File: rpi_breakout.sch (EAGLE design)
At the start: 31 parts, among them Q1 BSS138, Q2 BSS138, U2 TXB0108, U3 TXB0108

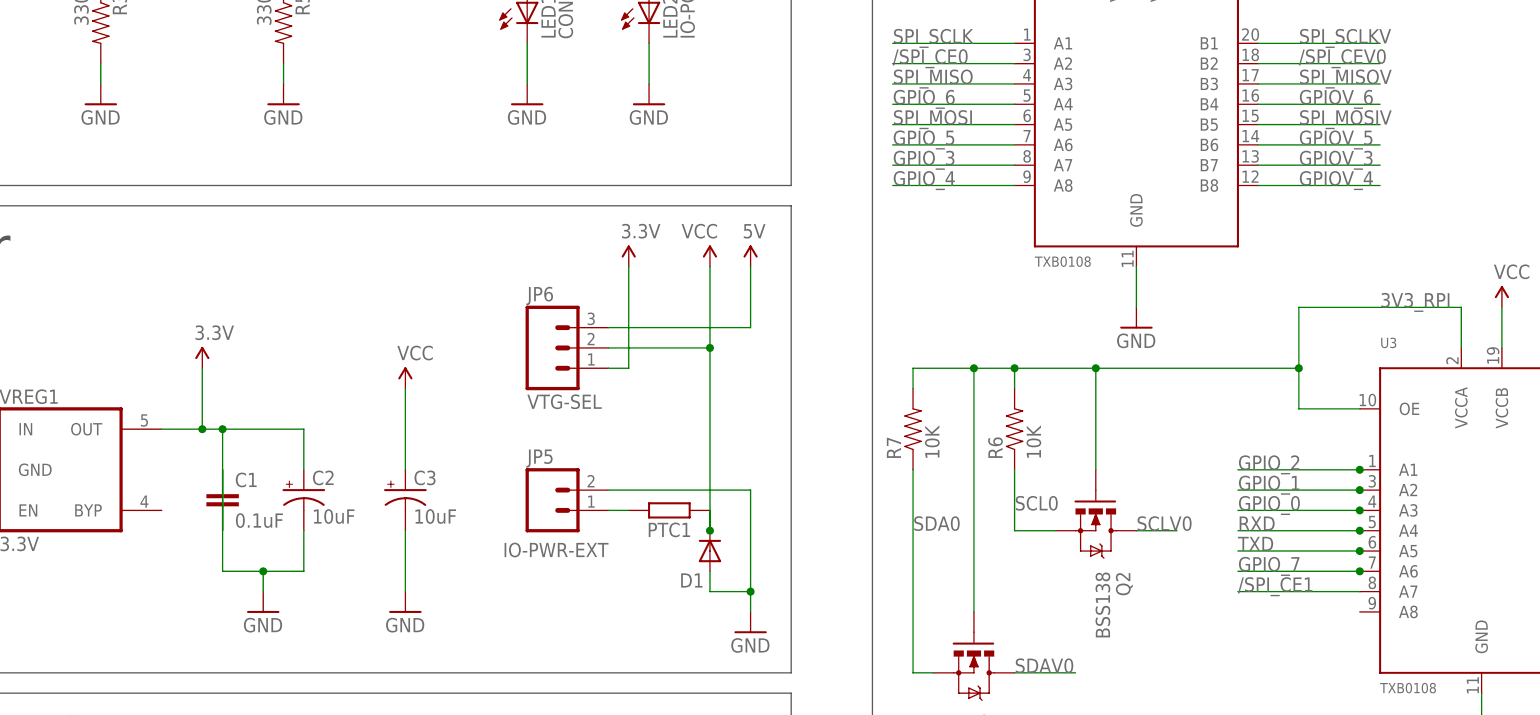
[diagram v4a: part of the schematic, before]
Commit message: Cleanup/routing after adding I2C-friendly level converter.
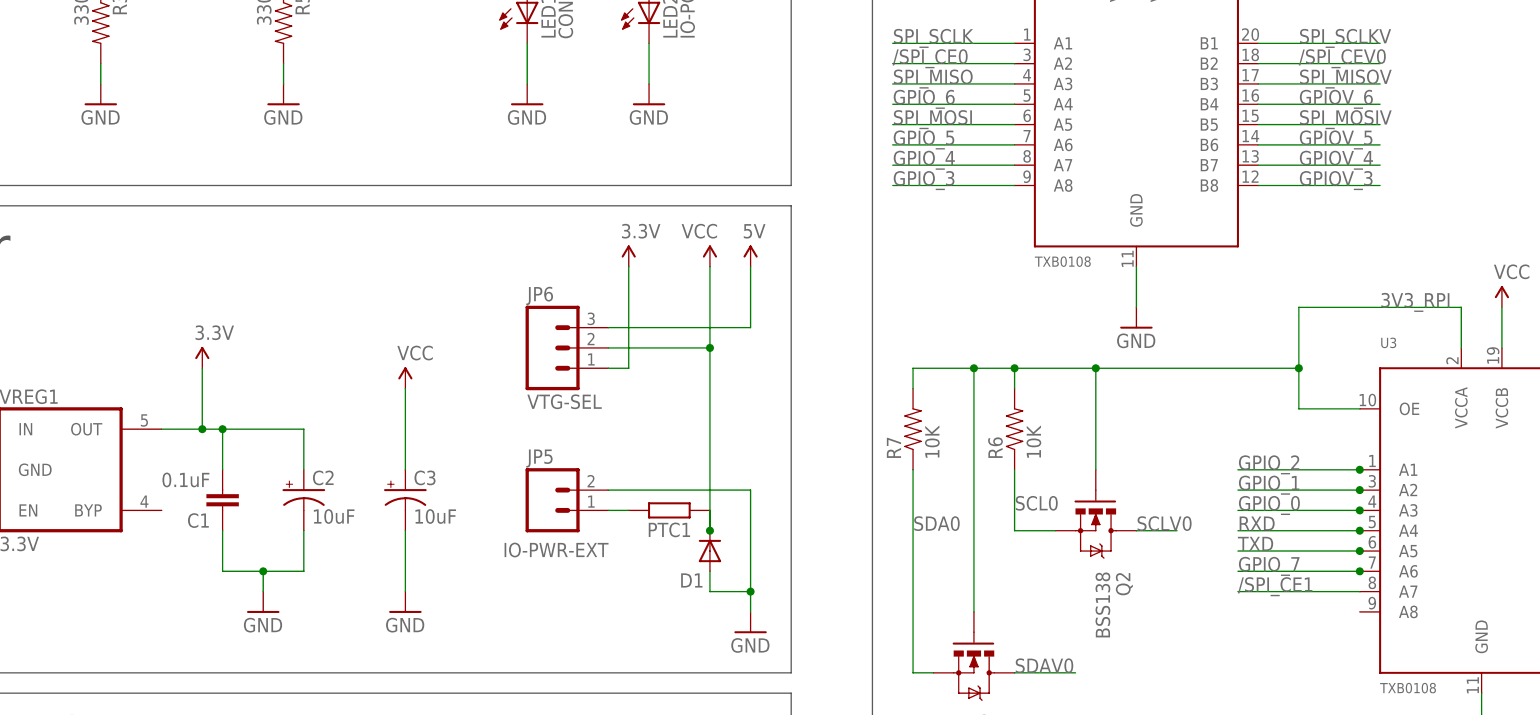
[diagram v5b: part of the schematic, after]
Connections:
- net GPIOV_3: now also U2.B8; no longer U2.B7
- net GPIOV_4: now also U2.B7; no longer U2.B8
- net GPIO_3: now also U2.A8; no longer U2.A7
- net GPIO_4: now also U2.A7; no longer U2.A8
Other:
- moved on the sheet: C1
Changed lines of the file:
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@@
 <instance part="GND8" gate="1" x="208.28" y="53.34"/>
 <instance part="VREG1" gate="G$1" x="30.48" y="88.9"/>
-<instance part="C1" gate="G$1" x="50.8" y="83.82"/>
+<instance part="C1" gate="G$1" x="50.8" y="86.36" rot="R180"/>
 <instance part="C2" gate="G$1" x="60.96" y="86.36"/>
 <instance part="GND9" gate="1" x="55.88" y="71.12"/>
@@
 <wire x1="55.88" y1="76.2" x2="55.88" y2="73.66" width="0.1524" layer="91"/>
 <pinref part="C1" gate="G$1" pin="1"/>
-<wire x1="50.8" y1="88.9" x2="50.8" y2="76.2" width="0.1524" layer="91"/>
+<wire x1="50.8" y1="81.28" x2="50.8" y2="76.2" width="0.1524" layer="91"/>
 <wire x1="50.8" y1="76.2" x2="55.88" y2="76.2" width="0.1524" layer="91"/>
 <junction x="55.88" y="76.2"/>
@@
 </segment>
 <segment>
-<pinref part="U2" gate="G$1" pin="A8"/>
-<wire x1="149.86" y1="124.46" x2="134.62" y2="124.46" width="0.1524" layer="91"/>
-<label x="134.62" y="124.46" size="1.778" layer="95" font="vector"/>
+<pinref part="U2" gate="G$1" pin="A7"/>
+<wire x1="149.86" y1="127" x2="134.62" y2="127" width="0.1524" layer="91"/>
+<label x="134.62" y="127" size="1.778" layer="95" font="vector"/>
 </segment>
 </net>
@@
 </segment>
 <segment>
-<pinref part="U2" gate="G$1" pin="A7"/>
-<wire x1="149.86" y1="127" x2="134.62" y2="127" width="0.1524" layer="91"/>
-<label x="134.62" y="127" size="1.778" layer="95" font="vector"/>
+<pinref part="U2" gate="G$1" pin="A8"/>
+<wire x1="149.86" y1="124.46" x2="134.62" y2="124.46" width="0.1524" layer="91"/>
+<label x="134.62" y="124.46" size="1.778" layer="95" font="vector"/>
 </segment>
 </net>
@@
 </segment>
 <segment>
+<pinref part="U2" gate="G$1" pin="B8"/>
+<wire x1="180.34" y1="124.46" x2="195.58" y2="124.46" width="0.1524" layer="91"/>
+<label x="185.42" y="124.46" size="1.778" layer="95" font="vector"/>
+</segment>
+</net>
+<net name="GPIOV_4" class="0">
+<segment>
+<pinref part="JP2" gate="G$1" pin="5"/>
+<wire x1="17.78" y1="33.02" x2="30.48" y2="33.02" width="0.1524" layer="91"/>
+<label x="20.32" y="33.02" size="1.778" layer="95" font="vector"/>
+</segment>
+<segment>
 <pinref part="U2" gate="G$1" pin="B7"/>
 <wire x1="180.34" y1="127" x2="195.58" y2="127" width="0.1524" layer="91"/>
 <label x="185.42" y="127" size="1.778" layer="95" font="vector"/>
-</segment>
-</net>
-<net name="GPIOV_4" class="0">
-<segment>
-<pinref part="JP2" gate="G$1" pin="5"/>
-<wire x1="17.78" y1="33.02" x2="30.48" y2="33.02" width="0.1524" layer="91"/>
-<label x="20.32" y="33.02" size="1.778" layer="95" font="vector"/>
-</segment>
-<segment>
-<pinref part="U2" gate="G$1" pin="B8"/>
-<wire x1="180.34" y1="124.46" x2="195.58" y2="124.46" width="0.1524" layer="91"/>
-<label x="185.42" y="124.46" size="1.778" layer="95" font="vector"/>
 </segment>
 </net>
@@
 <wire x1="48.26" y1="93.98" x2="43.18" y2="93.98" width="0.1524" layer="91"/>
 <pinref part="C1" gate="G$1" pin="2"/>
-<wire x1="50.8" y1="81.28" x2="50.8" y2="93.98" width="0.1524" layer="91"/>
+<wire x1="50.8" y1="88.9" x2="50.8" y2="93.98" width="0.1524" layer="91"/>
 <pinref part="C2" gate="G$1" pin="+"/>
 <wire x1="50.8" y1="93.98" x2="60.96" y2="93.98" width="0.1524" layer="91"/>
